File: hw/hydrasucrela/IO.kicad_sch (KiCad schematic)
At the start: 4 parts, among them J1 Conn_02x20_Odd_Even, J2 Conn_02x05_Odd_Even, J3 Conn_02x05_Odd_Even, J4 Conn_01x05

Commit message: hw: update kicad footprints and symbols
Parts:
- J1: footprint (none) -> Connector_Harwin:Harwin_M20-7812045_2x20_P2.54mm_Vertical
- J2, J3: footprint (none) -> Connector_Harwin:Harwin_M20-7810545_2x05_P2.54mm_Vertical
- J4: footprint (none) -> Connector_PinSocket_2.54mm:PinSocket_1x05_P2.54mm_Vertical
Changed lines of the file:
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@@
 			)
 		)
-		(property "Footprint" ""
+		(property "Footprint" "Connector_Harwin:Harwin_M20-7810545_2x05_P2.54mm_Vertical"
 			(at 177.8 67.31 0)
 			(effects
@@
 			)
 		)
-		(property "Footprint" ""
+		(property "Footprint" "Connector_Harwin:Harwin_M20-7810545_2x05_P2.54mm_Vertical"
 			(at 237.49 67.31 0)
 			(effects
@@
 			)
 		)
-		(property "Footprint" ""
+		(property "Footprint" "Connector_Harwin:Harwin_M20-7812045_2x20_P2.54mm_Vertical"
 			(at 115.57 85.09 0)
 			(effects
@@
 			)
 		)
-		(property "Footprint" ""
+		(property "Footprint" "Connector_PinSocket_2.54mm:PinSocket_1x05_P2.54mm_Vertical"
 			(at 238.76 107.95 0)
 			(effects

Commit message: Update HydraSucreLA PCB
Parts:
- added J5: Conn_02x20_Top_Bottom, Library:probe_connector, symbol Connector_Generic:Conn_02x20_Counter_Clockwise
- J1: symbol Connector_Generic:Conn_02x20_Odd_Even -> Connector_Generic:Conn_02x20_Top_Bottom
- J2, J3: symbol Connector_Generic:Conn_02x05_Odd_Even -> Connector_Generic:Conn_02x05_Top_Bottom
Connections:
- net 3V3_IN: now also J3.6 (Pin_6); no longer J3.2 (Pin_2)
- net GND: now also J2.4 (Pin_4), J2.5 (Pin_5), J2.6 (Pin_6), J3.2 (Pin_2), J3.7 (Pin_7), J3.8 (Pin_8), J5.10 (Pin_10), J5.15 (Pin_15), J5.20 (Pin_20), J5.21 (Pin_21), J5.22 (Pin_22), J5.23 (Pin_23), J5.24 (Pin_24), J5.25 (Pin_25), J5.26 (Pin_26), J5.27 (Pin_27), J5.28 (Pin_28), J5.29 (Pin_29), J5.30 (Pin_30), J5.31 (Pin_31), J5.32 (Pin_32), J5.33 (Pin_33), J5.34 (Pin_34), J5.35 (Pin_35), J5.36 (Pin_36), J5.37 (Pin_37), J5.38 (Pin_38), J5.39 (Pin_39), J5.40 (Pin_40), J5.5 (Pin_5); no longer J2.2 (Pin_2), J2.7 (Pin_7), J2.9 (Pin_9), J3.4 (Pin_4), J3.6 (Pin_6), J3.9 (Pin_9)
- net HD0: now also J1.16 (Pin_16); no longer J1.31 (Pin_31)
- net HD1: now also J1.36 (Pin_36); no longer J1.32 (Pin_32)
- net HD10: now also J1.11 (Pin_11); no longer J1.21 (Pin_21)
- net HD11: now also J1.31 (Pin_31); no longer J1.22 (Pin_22)
- net HD12: now also J1.10 (Pin_10); no longer J1.19 (Pin_19)
- net HD13: now also J1.30 (Pin_30); no longer J1.20 (Pin_20)
- net HD14: now also J1.9 (Pin_9); no longer J1.17 (Pin_17)
- net HD15: now also J1.29 (Pin_29); no longer J1.18 (Pin_18)
- net HD16: now also J1.8 (Pin_8); no longer J1.15 (Pin_15)
- net HD17: now also J1.28 (Pin_28); no longer J1.16 (Pin_16)
- net HD18: now also J1.7 (Pin_7); no longer J1.13 (Pin_13)
- net HD19: now also J1.27 (Pin_27); no longer J1.14 (Pin_14)
- net HD2: now also J1.15 (Pin_15); no longer J1.29 (Pin_29)
- net HD20: now also J1.6 (Pin_6); no longer J1.11 (Pin_11)
- net HD21: now also J1.26 (Pin_26); no longer J1.12 (Pin_12)
- net HD22: now also J1.5 (Pin_5); no longer J1.9 (Pin_9)
- net HD23: now also J1.25 (Pin_25); no longer J1.10 (Pin_10)
- net HD24: now also J1.4 (Pin_4); no longer J1.7 (Pin_7)
- net HD25: now also J1.24 (Pin_24); no longer J1.8 (Pin_8)
- net HD26: now also J1.3 (Pin_3); no longer J1.5 (Pin_5)
- net HD27: now also J1.23 (Pin_23); no longer J1.6 (Pin_6)
- net HD28: now also J1.2 (Pin_2); no longer J1.3 (Pin_3)
- net HD29: now also J1.22 (Pin_22); no longer J1.4 (Pin_4)
- net HD3: now also J1.35 (Pin_35); no longer J1.30 (Pin_30)
- net HD31: now also J1.21 (Pin_21); no longer J1.2 (Pin_2)
- net HD4: now also J1.14 (Pin_14); no longer J1.27 (Pin_27)
- net HD5: now also J1.34 (Pin_34); no longer J1.28 (Pin_28)
- net HD6: now also J1.13 (Pin_13); no longer J1.25 (Pin_25)
- net HD7: now also J1.33 (Pin_33); no longer J1.26 (Pin_26)
- net HD8: now also J1.12 (Pin_12); no longer J1.23 (Pin_23)
- net HD9: now also J1.32 (Pin_32); no longer J1.24 (Pin_24)
- net HRACT: now also J1.38 (Pin_38); no longer J1.36 (Pin_36)
- net HRCLK: now also J1.18 (Pin_18); no longer J1.35 (Pin_35)
- net HRVLD: now also J1.37 (Pin_37); no longer J1.34 (Pin_34)
- net HTACK: now also J1.17 (Pin_17); no longer J1.33 (Pin_33)
- net HTCLK: now also J1.20 (Pin_20); no longer J1.39 (Pin_39)
- net HTRDY: now also J1.19 (Pin_19); no longer J1.37 (Pin_37)
- net HTVLD: now also J1.39 (Pin_39); no longer J1.38 (Pin_38)
- net MISO0: now also J2.8 (Pin_8); no longer J2.6 (Pin_6)
- net MOSI0: now also J2.3 (Pin_3); no longer J2.5 (Pin_5)
- net P5.0V: now also J2.9 (Pin_9); no longer J2.8 (Pin_8)
- net RXD_1: now also J3.4 (Pin_4); no longer J3.7 (Pin_7)
- net SCK0: now also J2.7 (Pin_7); no longer J2.4 (Pin_4)
- net SCS0: now also J2.2 (Pin_2); no longer J2.3 (Pin_3)
- net TXD_1: now also J3.9 (Pin_9); no longer J3.8 (Pin_8)
- new net Probe_0: J5.1 (Pin_1)
- new net Probe_1: J5.2 (Pin_2)
- new net Probe_10: J5.13 (Pin_13)
- new net Probe_11: J5.14 (Pin_14)
- new net Probe_12: J5.16 (Pin_16)
- new net Probe_13: J5.17 (Pin_17)
- new net Probe_14: J5.18 (Pin_18)
- new net Probe_15: J5.19 (Pin_19)
- new net Probe_2: J5.3 (Pin_3)
- new net Probe_3: J5.4 (Pin_4)
- new net Probe_4: J5.6 (Pin_6)
- new net Probe_5: J5.7 (Pin_7)
- new net Probe_6: J5.8 (Pin_8)
- new net Probe_7: J5.9 (Pin_9)
- new net Probe_8: J5.11 (Pin_11)
- new net Probe_9: J5.12 (Pin_12)
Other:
- note added: "Probe connector (female)"

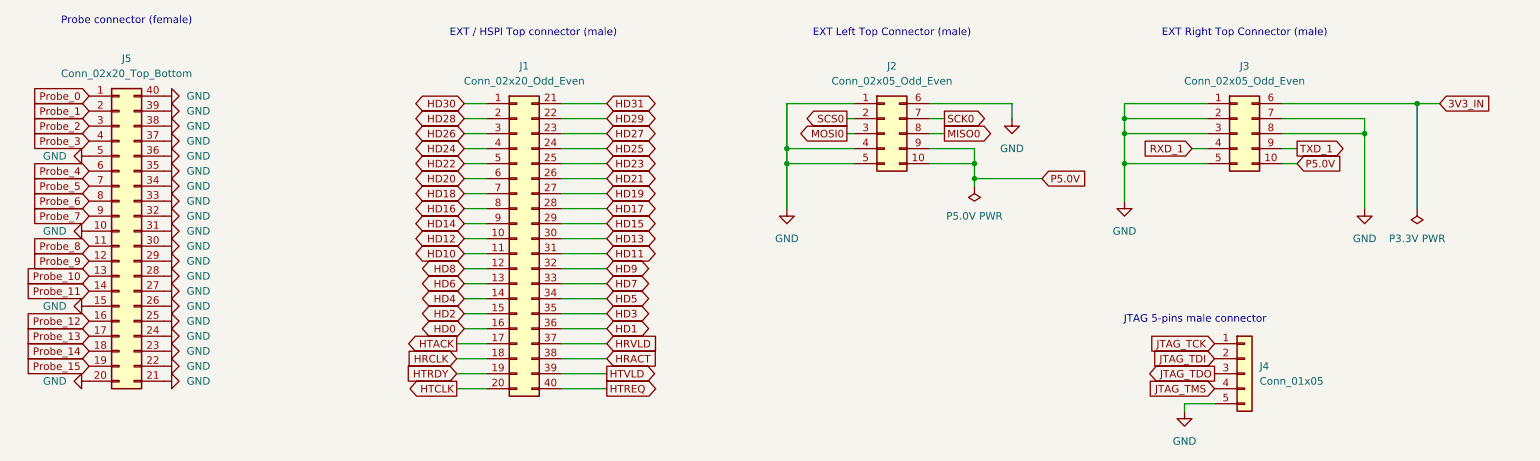
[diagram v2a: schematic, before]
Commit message: update PCB with good connector placements
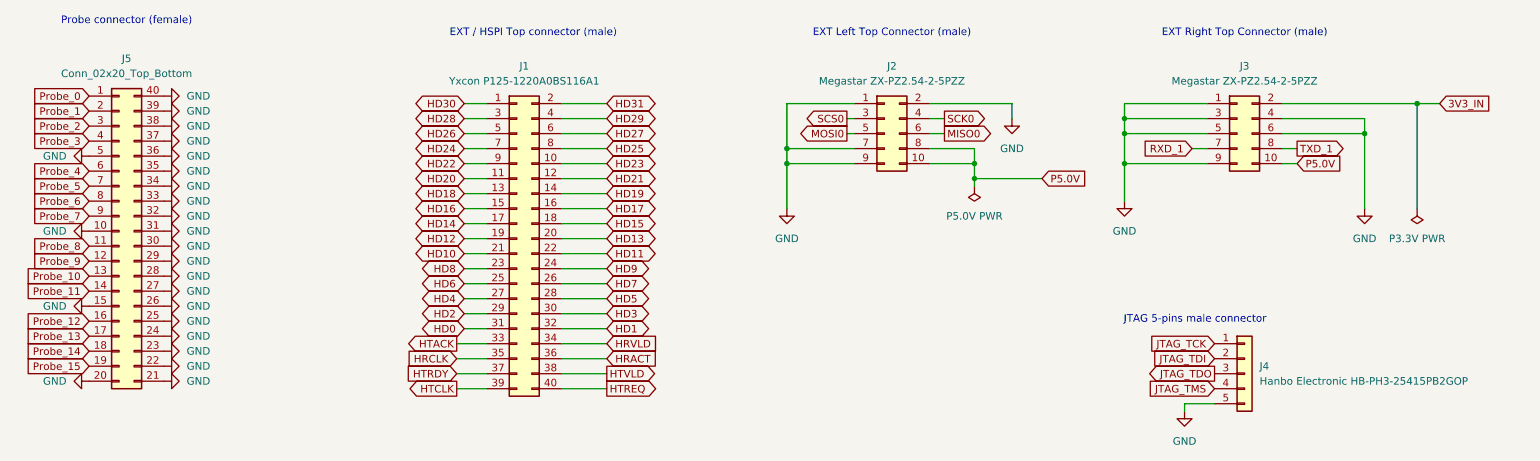
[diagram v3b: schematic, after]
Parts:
- J1: value Conn_02x20_Odd_Even -> Yxcon P125-1220A0BS116A1; footprint Connector_Harwin:Harwin_M20-7812045_2x20_P2.54mm_Vertical -> Connector_PinHeader_2.54mm:PinHeader_2x20_P2.54mm_Vertical; symbol Connector_Generic:Conn_02x20_Top_Bottom -> Connector_Generic:Conn_02x20_Odd_Even
- J2, J3: value Conn_02x05_Odd_Even -> Megastar ZX-PZ2.54-2-5PZZ; footprint Connector_Harwin:Harwin_M20-7810545_2x05_P2.54mm_Vertical -> Connector_PinHeader_2.54mm:PinHeader_2x05_P2.54mm_Vertical; symbol Connector_Generic:Conn_02x05_Top_Bottom -> Connector_Generic:Conn_02x05_Odd_Even
- J4: value Conn_01x05 -> Hanbo Electronic HB-PH3-25415PB2GOP
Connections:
- net 3V3_IN: now also J3.2 (Pin_2); no longer J3.6 (Pin_6)
- net GND: now also J2.2 (Pin_2), J2.7 (Pin_7), J2.9 (Pin_9), J3.4 (Pin_4), J3.6 (Pin_6), J3.9 (Pin_9); no longer J2.4 (Pin_4), J2.5 (Pin_5), J2.6 (Pin_6), J3.2 (Pin_2), J3.7 (Pin_7), J3.8 (Pin_8)
- net HD0: now also J1.31 (Pin_31); no longer J1.16 (Pin_16)
- net HD1: now also J1.32 (Pin_32); no longer J1.36 (Pin_36)
- net HD10: now also J1.21 (Pin_21); no longer J1.11 (Pin_11)
- net HD11: now also J1.22 (Pin_22); no longer J1.31 (Pin_31)
- net HD12: now also J1.19 (Pin_19); no longer J1.10 (Pin_10)
- net HD13: now also J1.20 (Pin_20); no longer J1.30 (Pin_30)
- net HD14: now also J1.17 (Pin_17); no longer J1.9 (Pin_9)
- net HD15: now also J1.18 (Pin_18); no longer J1.29 (Pin_29)
- net HD16: now also J1.15 (Pin_15); no longer J1.8 (Pin_8)
- net HD17: now also J1.16 (Pin_16); no longer J1.28 (Pin_28)
- net HD18: now also J1.13 (Pin_13); no longer J1.7 (Pin_7)
- net HD19: now also J1.14 (Pin_14); no longer J1.27 (Pin_27)
- net HD2: now also J1.29 (Pin_29); no longer J1.15 (Pin_15)
- net HD20: now also J1.11 (Pin_11); no longer J1.6 (Pin_6)
- net HD21: now also J1.12 (Pin_12); no longer J1.26 (Pin_26)
- net HD22: now also J1.9 (Pin_9); no longer J1.5 (Pin_5)
- net HD23: now also J1.10 (Pin_10); no longer J1.25 (Pin_25)
- net HD24: now also J1.7 (Pin_7); no longer J1.4 (Pin_4)
- net HD25: now also J1.8 (Pin_8); no longer J1.24 (Pin_24)
- net HD26: now also J1.5 (Pin_5); no longer J1.3 (Pin_3)
- net HD27: now also J1.6 (Pin_6); no longer J1.23 (Pin_23)
- net HD28: now also J1.3 (Pin_3); no longer J1.2 (Pin_2)
- net HD29: now also J1.4 (Pin_4); no longer J1.22 (Pin_22)
- net HD3: now also J1.30 (Pin_30); no longer J1.35 (Pin_35)
- net HD31: now also J1.2 (Pin_2); no longer J1.21 (Pin_21)
- net HD4: now also J1.27 (Pin_27); no longer J1.14 (Pin_14)
- net HD5: now also J1.28 (Pin_28); no longer J1.34 (Pin_34)
- net HD6: now also J1.25 (Pin_25); no longer J1.13 (Pin_13)
- net HD7: now also J1.26 (Pin_26); no longer J1.33 (Pin_33)
- net HD8: now also J1.23 (Pin_23); no longer J1.12 (Pin_12)
- net HD9: now also J1.24 (Pin_24); no longer J1.32 (Pin_32)
- net HRACT: now also J1.36 (Pin_36); no longer J1.38 (Pin_38)
- net HRCLK: now also J1.35 (Pin_35); no longer J1.18 (Pin_18)
- net HRVLD: now also J1.34 (Pin_34); no longer J1.37 (Pin_37)
- net HTACK: now also J1.33 (Pin_33); no longer J1.17 (Pin_17)
- net HTCLK: now also J1.39 (Pin_39); no longer J1.20 (Pin_20)
- net HTRDY: now also J1.37 (Pin_37); no longer J1.19 (Pin_19)
- net HTVLD: now also J1.38 (Pin_38); no longer J1.39 (Pin_39)
- net MISO0: now also J2.6 (Pin_6); no longer J2.8 (Pin_8)
- net MOSI0: now also J2.5 (Pin_5); no longer J2.3 (Pin_3)
- net P5.0V: now also J2.8 (Pin_8); no longer J2.9 (Pin_9)
- net RXD_1: now also J3.7 (Pin_7); no longer J3.4 (Pin_4)
- net SCK0: now also J2.4 (Pin_4); no longer J2.7 (Pin_7)
- net SCS0: now also J2.3 (Pin_3); no longer J2.2 (Pin_2)
- net TXD_1: now also J3.8 (Pin_8); no longer J3.9 (Pin_9)
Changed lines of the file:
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@@
 	)
 	(symbol
-		(lib_id "Connector_Generic:Conn_02x05_Top_Bottom")
+		(lib_id "Connector_Generic:Conn_02x05_Odd_Even")
 		(at 177.8 67.31 0)
 		(unit 1)
@@
 			)
 		)
-		(property "Value" "Conn_02x05_Odd_Even"
+		(property "Value" "Megastar ZX-PZ2.54-2-5PZZ"
 			(at 179.07 58.42 0)
 			(effects
@@
 			)
 		)
-		(property "Footprint" "Connector_Harwin:Harwin_M20-7810545_2x05_P2.54mm_Vertical"
+		(property "Footprint" "Connector_PinHeader_2.54mm:PinHeader_2x05_P2.54mm_Vertical"
 			(at 177.8 67.31 0)
 			(effects
@@
 			)
 		)
-		(property "Datasheet" "~"
+		(property "Datasheet" "https://www.lcsc.com/datasheet/lcsc_datasheet_2311221544_Megastar-ZX-PZ2-54-2-5PZZ_C7501276.pdf"
 			(at 177.8 67.31 0)
 			(effects
@@
 			)
 		)
-		(property "Description" "Generic connector, double row, 02x05, top/bottom pin numbering scheme (row 1: 1...pins_per_row, row2: pins_per_row+1 ... num_pins), script generated (kicad-library-utils/schlib/autogen/connector/)"
+		(property "Description" "Generic connector, double row, 02x05, odd/even pin numbering scheme (row 1 odd numbers, row 2 even numbers), script generated (kicad-library-utils/schlib/autogen/connector/)"
 			(at 177.8 67.31 0)
 			(effects
@@
 	)
 	(symbol
-		(lib_id "Connector_Generic:Conn_02x05_Top_Bottom")
+		(lib_id "Connector_Generic:Conn_02x05_Odd_Even")
 		(at 237.49 67.31 0)
 		(unit 1)
@@
 			)
 		)
-		(property "Value" "Conn_02x05_Odd_Even"
+		(property "Value" "Megastar ZX-PZ2.54-2-5PZZ"
 			(at 238.76 58.42 0)
 			(effects
@@
 			)
 		)
-		(property "Footprint" "Connector_Harwin:Harwin_M20-7810545_2x05_P2.54mm_Vertical"
+		(property "Footprint" "Connector_PinHeader_2.54mm:PinHeader_2x05_P2.54mm_Vertical"
 			(at 237.49 67.31 0)
 			(effects
@@
 			)
 		)
-		(property "Description" "Generic connector, double row, 02x05, top/bottom pin numbering scheme (row 1: 1...pins_per_row, row2: pins_per_row+1 ... num_pins), script generated (kicad-library-utils/schlib/autogen/connector/)"
+		(property "Description" "Generic connector, double row, 02x05, odd/even pin numbering scheme (row 1 odd numbers, row 2 even numbers), script generated (kicad-library-utils/schlib/autogen/connector/)"
 			(at 237.49 67.31 0)
 			(effects
@@
 	)
 	(symbol
-		(lib_id "Connector_Generic:Conn_02x20_Top_Bottom")
+		(lib_id "Connector_Generic:Conn_02x20_Odd_Even")
 		(at 115.57 85.09 0)
 		(unit 1)
@@
 			)
 		)
-		(property "Value" "Conn_02x20_Odd_Even"
+		(property "Value" "Yxcon P125-1220A0BS116A1"
 			(at 116.84 58.42 0)
 			(effects
@@
 			)
 		)
-		(property "Footprint" "Connector_Harwin:Harwin_M20-7812045_2x20_P2.54mm_Vertical"
+		(property "Footprint" "Connector_PinHeader_2.54mm:PinHeader_2x20_P2.54mm_Vertical"
 			(at 115.57 85.09 0)
 			(effects
@@
 			)
 		)
-		(property "Datasheet" "~"
+		(property "Datasheet" "https://www.lcsc.com/datasheet/lcsc_datasheet_2403231322_Yxcon-P125-1220A0BS116A1_C19190512.pdf"
 			(at 115.57 85.09 0)
 			(effects
@@
 			)
 		)
-		(property "Description" "Generic connector, double row, 02x20, top/bottom pin numbering scheme (row 1: 1...pins_per_row, row2: pins_per_row+1 ... num_pins), script generated (kicad-library-utils/schlib/autogen/connector/)"
+		(property "Description" "Generic connector, double row, 02x20, odd/even pin numbering scheme (row 1 odd numbers, row 2 even numbers), script generated (kicad-library-utils/schlib/autogen/connector/)"
 			(at 115.57 85.09 0)
 			(effects
@@
 			)
 		)
-		(property "Value" "Conn_01x05"
+		(property "Value" "Hanbo Electronic HB-PH3-25415PB2GOP"
 			(at 241.3 109.2199 0)
 			(effects
@@
 			)
 		)
-		(property "Datasheet" "~"
+		(property "Datasheet" "https://www.lcsc.com/datasheet/lcsc_datasheet_2312301326_Hanbo-Electronic-HB-PH3-25415PB2GOP_C6332198.pdf"
 			(at 238.76 107.95 0)
 			(effects
